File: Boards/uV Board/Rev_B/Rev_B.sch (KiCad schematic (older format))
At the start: 2 parts, among them J1 Left Connector, J2 Right Connector

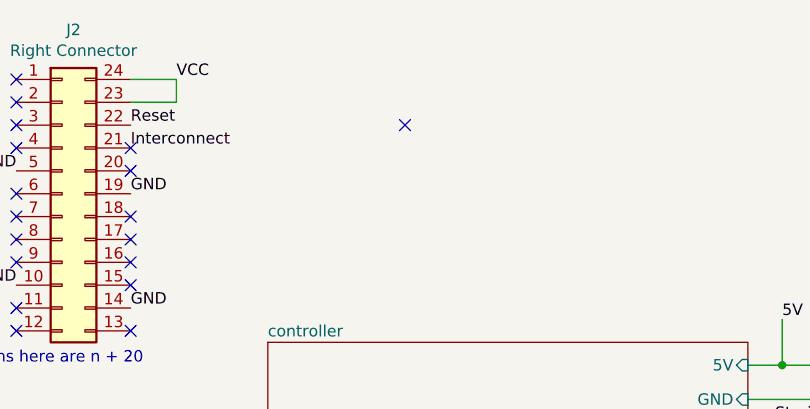
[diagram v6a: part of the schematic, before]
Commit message: In process of updating ADC board to remove 5V connection from PI. Also commiting small changes to uV board.
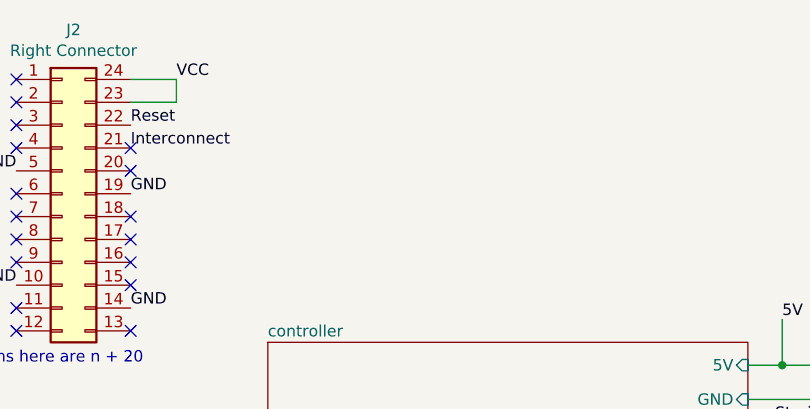
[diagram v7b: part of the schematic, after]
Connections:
- no-connect marks 28 -> 27
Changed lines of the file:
@@
 Wire Wire Line
 	8350 3900 8350 4300
-NoConn ~ 6350 1600
 $Sheet
 S 1850 3550 1200 900
